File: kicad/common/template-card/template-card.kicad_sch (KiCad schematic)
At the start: 18 parts, among them J1 Conn_01x06_Pin, J2 Conn_01x06_Pin, J4 Conn_01x05, U1 THVD1450DR, U2 STM32C011F4Px

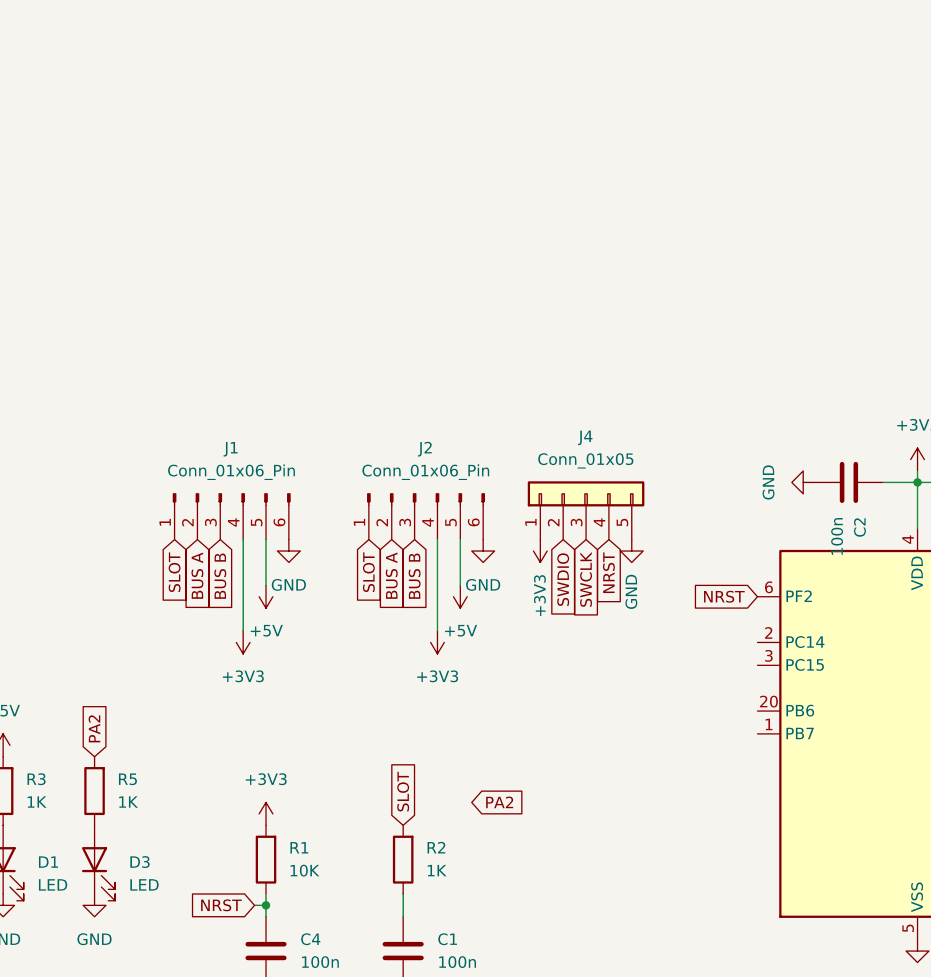
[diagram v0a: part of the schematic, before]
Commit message: Update card template and MIDI Buddy
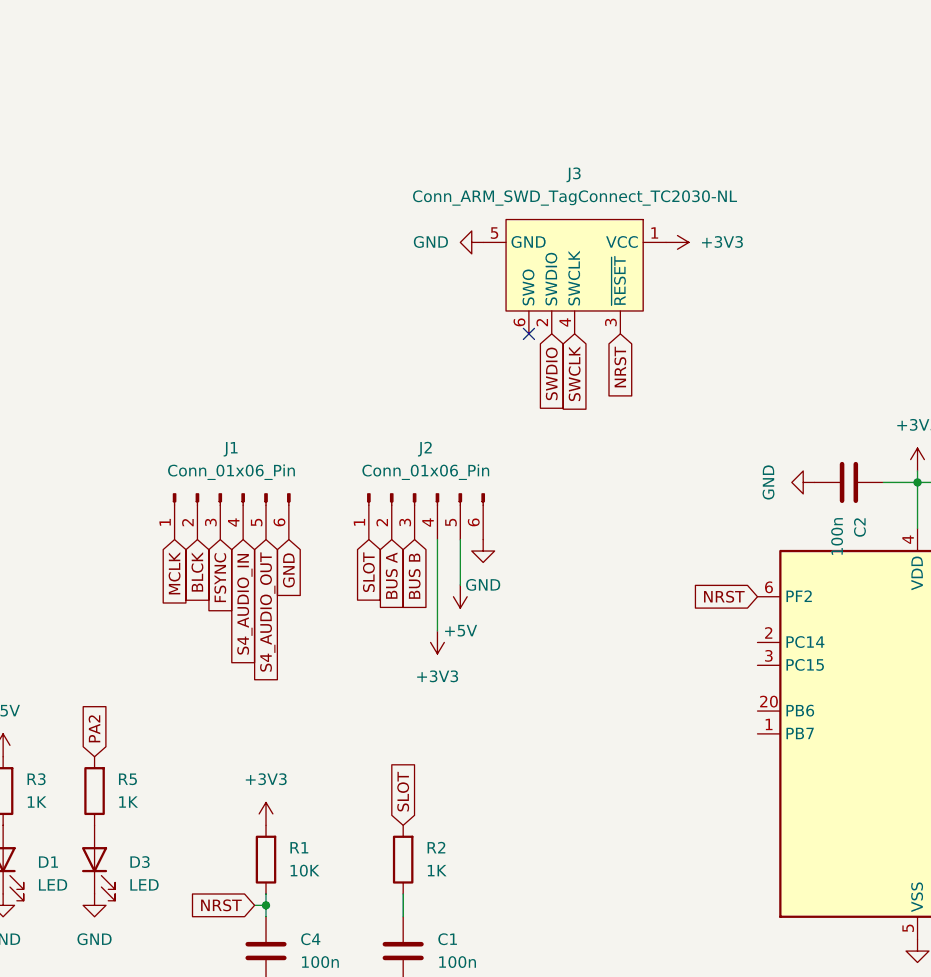
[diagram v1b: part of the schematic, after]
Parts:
- removed J4: Conn_01x05, Connector_PinHeader_1.27mm:PinHeader_1x05_P1.27mm_Vertical, symbol Connector_Generic:Conn_01x05
- added J3: Conn_ARM_SWD_TagConnect_TC2030-NL, Connector:Tag-Connect_TC2030-IDC-NL_2x03_P1.27mm_Vertical, symbol Connector:Conn_ARM_SWD_TagConnect_TC2030-NL
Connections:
- net +3V3: now also J3.1 (VCC); no longer J1.4 (Pin_4)
- net +5V: no longer J1.5 (Pin_5)
- net BUS A: no longer J1.2 (Pin_2)
- net BUS B: no longer J1.3 (Pin_3)
- net GND: now also J3.5 (GND)
- net NRST: now also J3.3 (~{RESET})
- net SLOT: no longer J1.1 (Pin_1)
- net SWCLK: now also J3.4 (SWCLK)
- net SWDIO: now also J3.2 (SWDIO)
- new net BLCK: J1.2 (Pin_2)
- new net FSYNC: J1.3 (Pin_3)
- new net MCLK: J1.1 (Pin_1)
- new net S4_AUDIO_IN: J1.4 (Pin_4)
- new net S4_AUDIO_OUT: J1.5 (Pin_5)
- no-connect marks 0 -> 1
